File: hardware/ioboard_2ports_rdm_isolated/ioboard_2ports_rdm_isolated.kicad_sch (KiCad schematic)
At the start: 32 parts, among them J1 Conn_02x06_Odd_Even, J12 Conn_01x03, J2 XLR3, J3 XLR3, J4 8P8C, J5 8P8C, J6 Conn_01x03, J8 XLR3, J9 XLR3, U1 M24C64-RMN6TP, U2 CRE1S0505DC, U4 ADM2483xRW, U6 ADM2483xRW

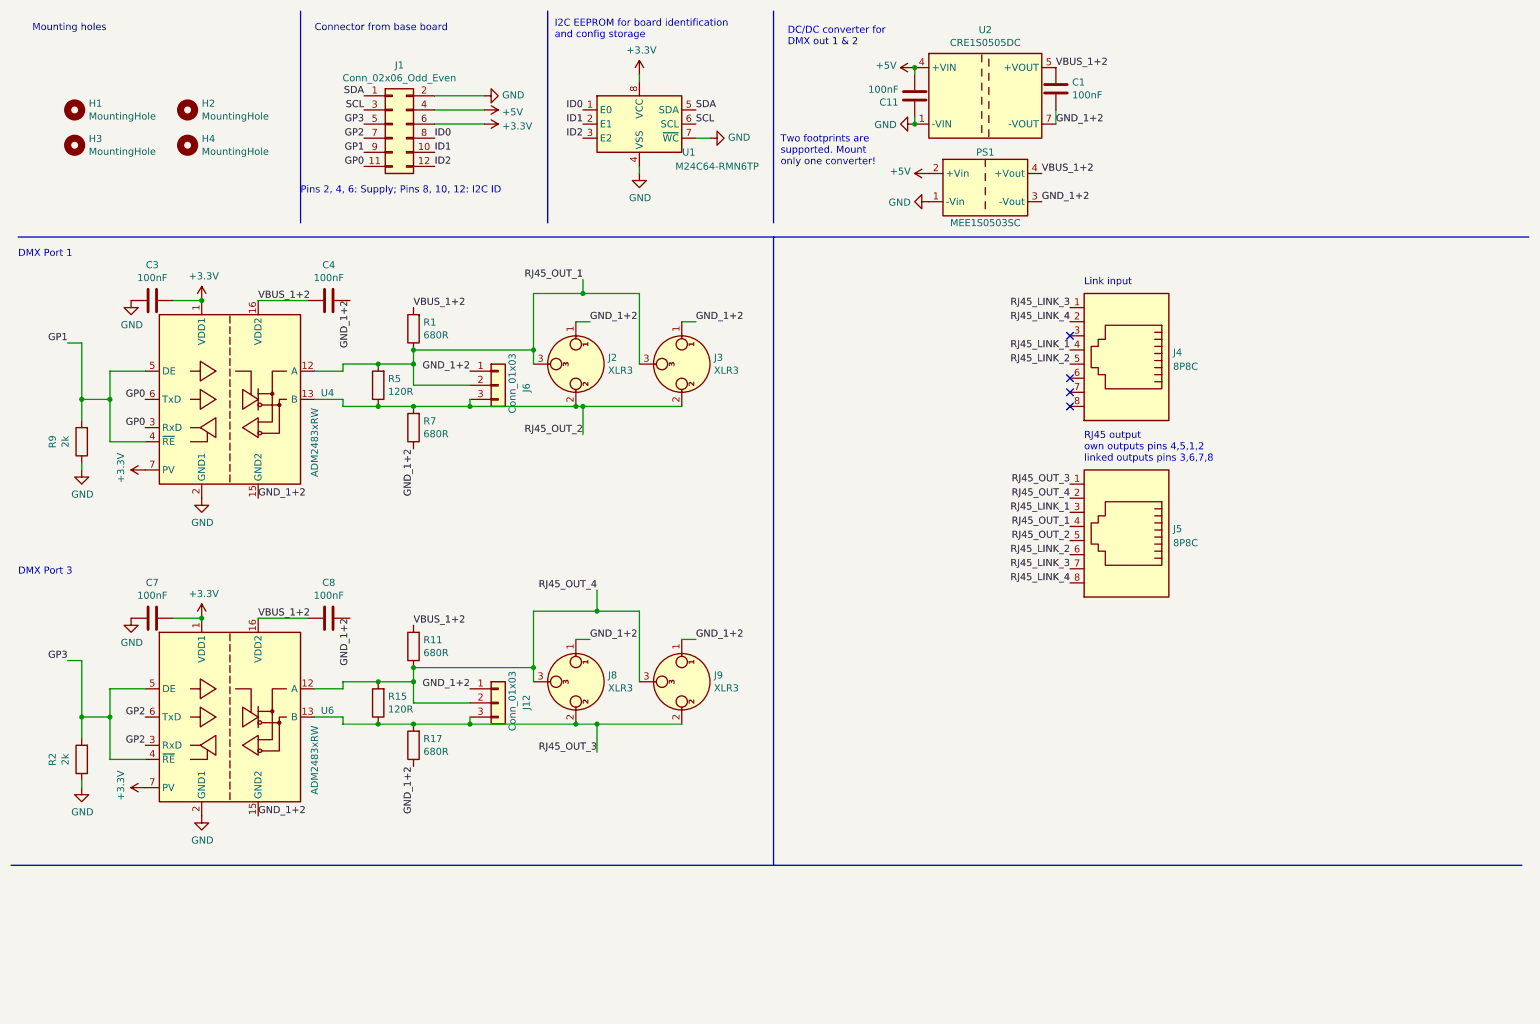
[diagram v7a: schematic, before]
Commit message: Update ioboards to KiCad 8, add OpenHardware logo
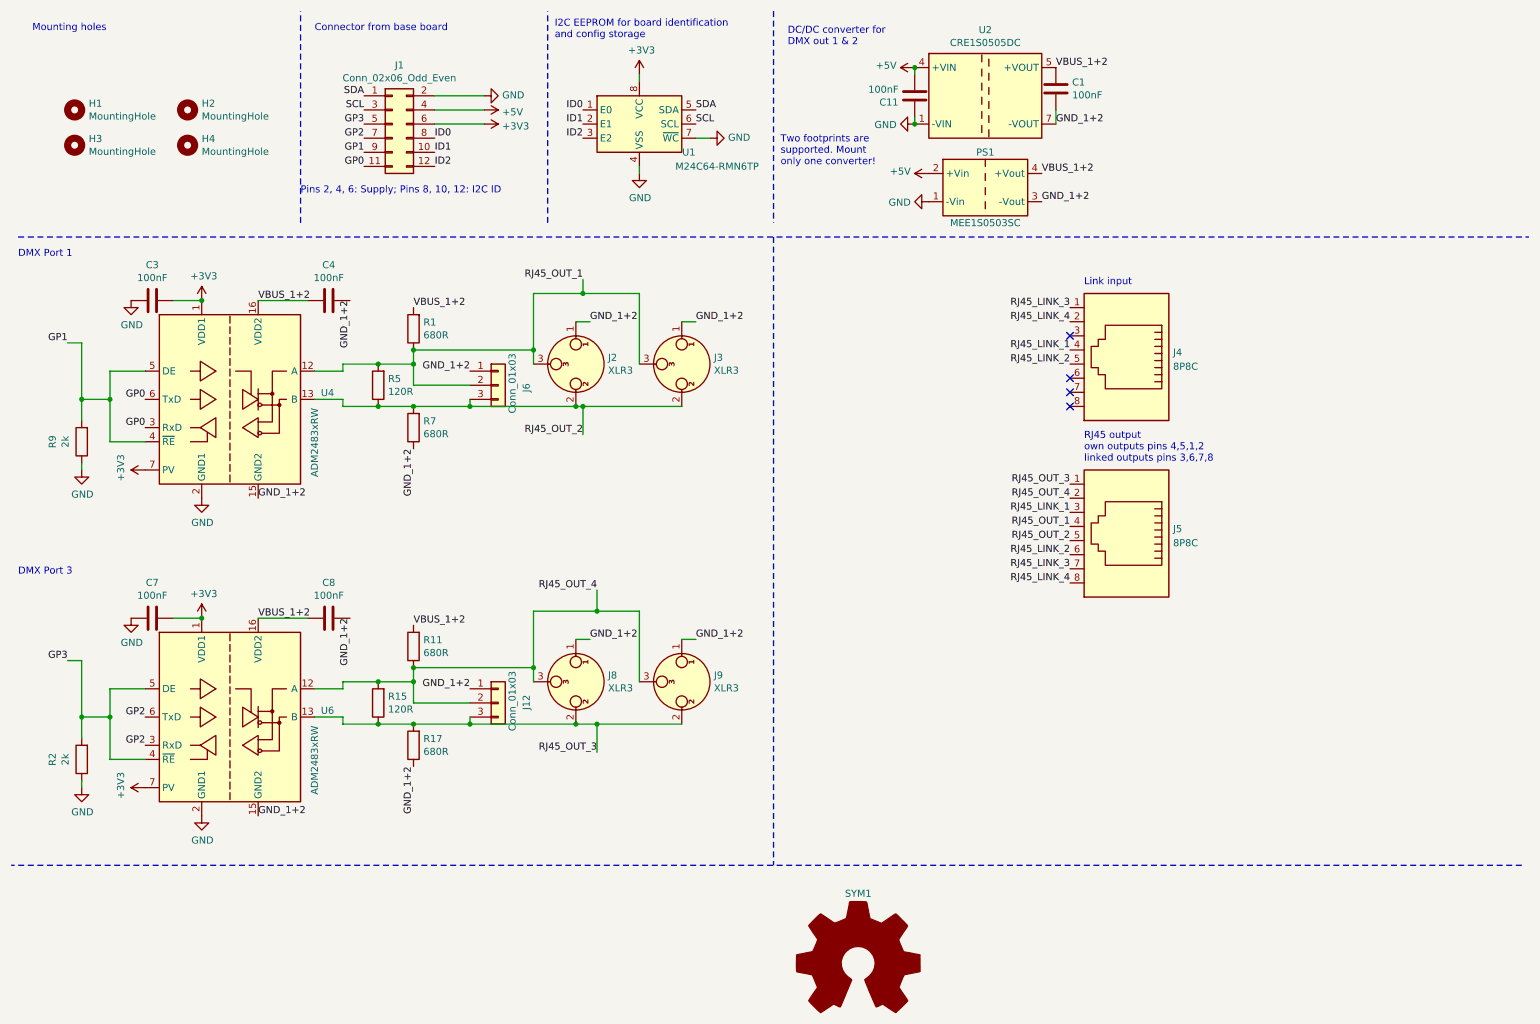
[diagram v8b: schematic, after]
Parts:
- added SYM1: Logo_Open_Hardware_Large, Symbol:OSHW-Logo2_14.6x12mm_SilkScreen, symbol Graphic:Logo_Open_Hardware_Large
